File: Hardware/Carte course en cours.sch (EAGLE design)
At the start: 41 parts, among them J2 AVR_SPI_PROG_3X2NS, J3 PWR IN, J4 RC receiver, J5 ESC, J6 ESC, J7 MICRO-SD_CARD_SOCKET, J8 ESC, U1 LM317, U2 ATMEGA328P_TQFP, U3 FT232RL, U4 MPU6050, Y1 16MHz

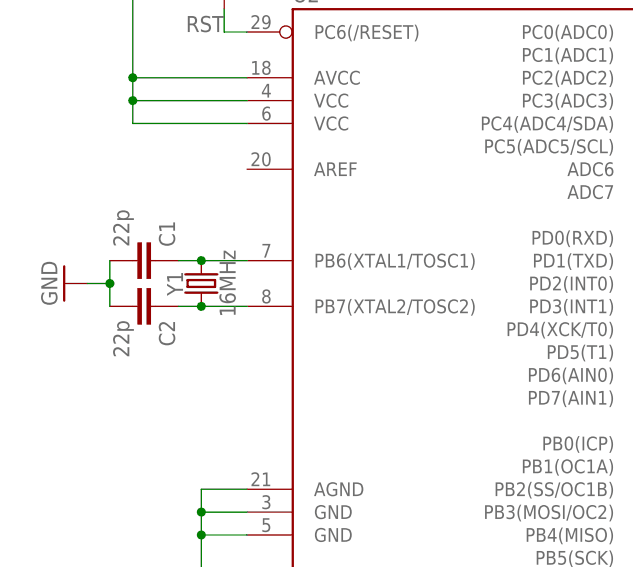
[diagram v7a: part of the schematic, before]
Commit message: Changed MCU frequency to 8MHz, to run safe at 3.3V
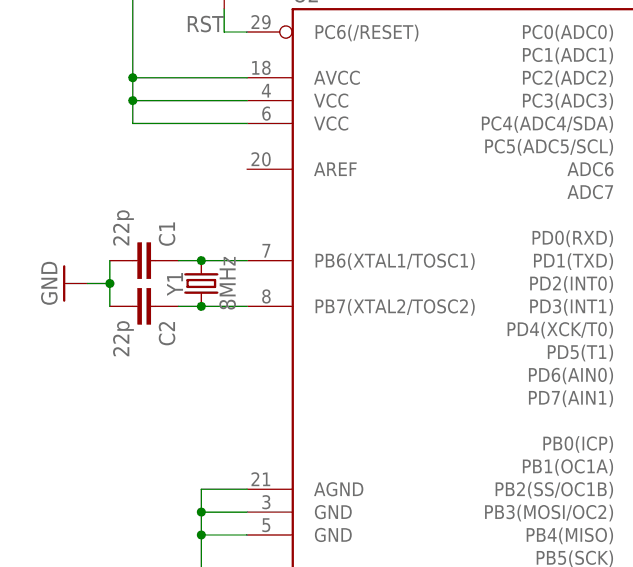
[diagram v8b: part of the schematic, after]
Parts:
- Y1: value 16MHz -> 8MHz; device SparkFun-Clocks:CRYSTAL-16MHZSMD-5X3.2 -> SparkFun-Clocks:CRYSTAL-8MHZSMD-5X3.2
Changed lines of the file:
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@@
 <?xml version="1.0" encoding="utf-8"?>
 <!DOCTYPE eagle SYSTEM "eagle.dtd">
-<eagle version="8.4.3">
+<eagle version="8.5.0">
 <drawing>
 <settings>
@@
 <grid distance="0.1" unitdist="inch" unit="inch" style="lines" multiple="1" display="no" altdistance="0.01" altunitdist="inch" altunit="inch"/>
 <layers>
-<layer number="1" name="Top" color="4" fill="1" visible="yes" active="no"/>
-<layer number="2" name="Route2" color="1" fill="3" visible="yes" active="no"/>
-<layer number="3" name="Route3" color="4" fill="3" visible="yes" active="no"/>
-<layer number="4" name="Route4" color="1" fill="4" visible="yes" active="no"/>
-<layer number="5" name="Route5" color="4" fill="4" visible="yes" active="no"/>
-<layer number="6" name="Route6" color="1" fill="8" visible="yes" active="no"/>
-<layer number="7" name="Route7" color="4" fill="8" visible="yes" active="no"/>
-<layer number="8" name="Route8" color="1" fill="2" visible="yes" active="no"/>
-<layer number="9" name="Route9" color="4" fill="2" visible="yes" active="no"/>
-<layer number="10" name="Route10" color="1" fill="7" visible="yes" active="no"/>
-<layer number="11" name="Route11" color="4" fill="7" visible="yes" active="no"/>
-<layer number="12" name="Route12" color="1" fill="5" visible="yes" active="no"/>
-<layer number="13" name="Route13" color="4" fill="5" visible="yes" active="no"/>
-<layer number="14" name="Route14" color="1" fill="6" visible="yes" active="no"/>
-<layer number="15" name="Route15" color="4" fill="6" visible="yes" active="no"/>
-<layer number="16" name="Bottom" color="1" fill="1" visible="yes" active="no"/>
-<layer number="17" name="Pads" color="2" fill="1" visible="yes" active="no"/>
-<layer number="18" name="Vias" color="2" fill="1" visible="yes" active="no"/>
-<layer number="19" name="Unrouted" color="6" fill="1" visible="yes" active="no"/>
-<layer number="20" name="Dimension" color="24" fill="1" visible="yes" active="no"/>
-<layer number="21" name="tPlace" color="7" fill="1" visible="yes" active="no"/>
-<layer number="22" name="bPlace" color="7" fill="1" visible="yes" active="no"/>
-<layer number="23" name="tOrigins" color="15" fill="1" visible="yes" active="no"/>
-<layer number="24" name="bOrigins" color="15" fill="1" visible="yes" active="no"/>
-<layer number="25" name="tNames" color="7" fill="1" visible="yes" active="no"/>
-<layer number="26" name="bNames" color="7" fill="1" visible="yes" active="no"/>
-<layer number="27" name="tValues" color="7" fill="1" visible="yes" active="no"/>
-<layer number="28" name="bValues" color="7" fill="1" visible="yes" active="no"/>
+<layer number="1" name="Top" color="4" fill="1" visible="no" active="no"/>
+<layer number="2" name="Route2" color="1" fill="3" visible="no" active="no"/>
+<layer number="3" name="Route3" color="4" fill="3" visible="no" active="no"/>
+<layer number="4" name="Route4" color="1" fill="4" visible="no" active="no"/>
+<layer number="5" name="Route5" color="4" fill="4" visible="no" active="no"/>
+<layer number="6" name="Route6" color="1" fill="8" visible="no" active="no"/>
+<layer number="7" name="Route7" color="4" fill="8" visible="no" active="no"/>
+<layer number="8" name="Route8" color="1" fill="2" visible="no" active="no"/>
+<layer number="9" name="Route9" color="4" fill="2" visible="no" active="no"/>
+<layer number="10" name="Route10" color="1" fill="7" visible="no" active="no"/>
+<layer number="11" name="Route11" color="4" fill="7" visible="no" active="no"/>
+<layer number="12" name="Route12" color="1" fill="5" visible="no" active="no"/>
+<layer number="13" name="Route13" color="4" fill="5" visible="no" active="no"/>
+<layer number="14" name="Route14" color="1" fill="6" visible="no" active="no"/>
+<layer number="15" name="Route15" color="4" fill="6" visible="no" active="no"/>
+<layer number="16" name="Bottom" color="1" fill="1" visible="no" active="no"/>
+<layer number="17" name="Pads" color="2" fill="1" visible="no" active="no"/>
+<layer number="18" name="Vias" color="2" fill="1" visible="no" active="no"/>
+<layer number="19" name="Unrouted" color="6" fill="1" visible="no" active="no"/>
+<layer number="20" name="Dimension" color="24" fill="1" visible="no" active="no"/>
+<layer number="21" name="tPlace" color="7" fill="1" visible="no" active="no"/>
+<layer number="22" name="bPlace" color="7" fill="1" visible="no" active="no"/>
+<layer number="23" name="tOrigins" color="15" fill="1" visible="no" active="no"/>
+<layer number="24" name="bOrigins" color="15" fill="1" visible="no" active="no"/>
+<layer number="25" name="tNames" color="7" fill="1" visible="no" active="no"/>
+<layer number="26" name="bNames" color="7" fill="1" visible="no" active="no"/>
+<layer number="27" name="tValues" color="7" fill="1" visible="no" active="no"/>
+<layer number="28" name="bValues" color="7" fill="1" visible="no" active="no"/>
 <layer number="29" name="tStop" color="7" fill="3" visible="no" active="no"/>
 <layer number="30" name="bStop" color="7" fill="6" visible="no" active="no"/>
@@
 <layer number="35" name="tGlue" color="7" fill="4" visible="no" active="no"/>
 <layer number="36" name="bGlue" color="7" fill="5" visible="no" active="no"/>
-<layer number="37" name="tTest" color="7" fill="1" visible="yes" active="no"/>
-<layer number="38" name="bTest" color="7" fill="1" visible="yes" active="no"/>
+<layer number="37" name="tTest" color="7" fill="1" visible="no" active="no"/>
+<layer number="38" name="bTest" color="7" fill="1" visible="no" active="no"/>
 <layer number="39" name="tKeepout" color="4" fill="11" visible="no" active="no"/>
 <layer number="40" name="bKeepout" color="1" fill="11" visible="no" active="no"/>
@@
 <layer number="44" name="Drills" color="7" fill="1" visible="no" active="no"/>
 <layer number="45" name="Holes" color="7" fill="1" visible="no" active="no"/>
-<layer number="46" name="Milling" color="3" fill="1" visible="yes" active="no"/>
-<layer number="47" name="Measures" color="7" fill="1" visible="yes" active="no"/>
-<layer number="48" name="Document" color="7" fill="1" visible="yes" active="no"/>
-<layer number="49" name="Reference" color="7" fill="1" visible="yes" active="no"/>
-<layer number="50" name="dxf" color="7" fill="1" visible="yes" active="no"/>
-<layer number="51" name="tDocu" color="7" fill="1" visible="yes" active="no"/>
-<layer number="52" name="bDocu" color="7" fill="1" visible="yes" active="no"/>
-<layer number="53" name="tGND_GNDA" color="7" fill="9" visible="yes" active="no"/>
-<layer number="54" name="bGND_GNDA" color="1" fill="9" visible="yes" active="no"/>
-<layer number="56" name="wert" color="7" fill="1" visible="yes" active="no"/>
-<layer number="57" name="tCAD" color="7" fill="1" visible="yes" active="no"/>
-<layer number="59" name="tCarbon" color="7" fill="1" visible="yes" active="no"/>
-<layer number="60" name="bCarbon" color="7" fill="1" visible="yes" active="no"/>
+<layer number="46" name="Milling" color="3" fill="1" visible="no" active="no"/>
+<layer number="47" name="Measures" color="7" fill="1" visible="no" active="no"/>
+<layer number="48" name="Document" color="7" fill="1" visible="no" active="no"/>
+<layer number="49" name="Reference" color="7" fill="1" visible="no" active="no"/>
+<layer number="50" name="dxf" color="7" fill="1" visible="no" active="no"/>
+<layer number="51" name="tDocu" color="7" fill="1" visible="no" active="no"/>
+<layer number="52" name="bDocu" color="7" fill="1" visible="no" active="no"/>
+<layer number="53" name="tGND_GNDA" color="7" fill="9" visible="no" active="no"/>
+<layer number="54" name="bGND_GNDA" color="1" fill="9" visible="no" active="no"/>
+<layer number="56" name="wert" color="7" fill="1" visible="no" active="no"/>
+<layer number="57" name="tCAD" color="7" fill="1" visible="no" active="no"/>
+<layer number="59" name="tCarbon" color="7" fill="1" visible="no" active="no"/>
+<layer number="60" name="bCarbon" color="7" fill="1" visible="no" active="no"/>
 <layer number="88" name="SimResults" color="9" fill="1" visible="yes" active="yes"/>
 <layer number="89" name="SimProbes" color="9" fill="1" visible="yes" active="yes"/>
@@
 <part name="C1" library="rcl" library_urn="urn:adsk.eagle:library:334" deviceset="C-EU" device="C0805" package3d_urn="urn:adsk.eagle:package:23617/2" value="22p"/>
 <part name="C2" library="rcl" library_urn="urn:adsk.eagle:library:334" deviceset="C-EU" device="C0805" package3d_urn="urn:adsk.eagle:package:23617/2" value="22p"/>
-<part name="Y1" library="SparkFun-Clocks" library_urn="urn:adsk.eagle:library:511" deviceset="CRYSTAL-16MHZ" device="SMD-5X3.2" package3d_urn="urn:adsk.eagle:package:37518/1" value="16MHz"/>
+<part name="Y1" library="SparkFun-Clocks" deviceset="CRYSTAL-8MHZ" device="SMD-5X3.2" value="8MHz"/>
 <part name="GND2" library="supply1" library_urn="urn:adsk.eagle:library:371" deviceset="GND" device=""/>
 <part name="GND7" library="supply1" library_urn="urn:adsk.eagle:library:371" deviceset="GND" device=""/>
